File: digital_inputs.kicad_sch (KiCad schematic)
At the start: 4 parts, among them J3 Samtec Isorate, U7 SN74LV8T9541-EP

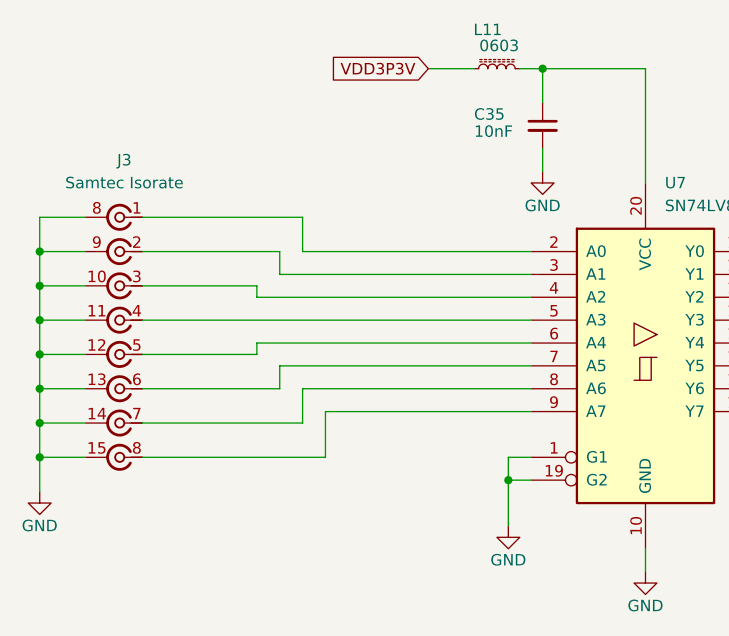
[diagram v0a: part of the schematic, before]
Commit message: Draft Schematic Complete
-See design.md for remaining design work/questions
-See output folder for current schematic prints
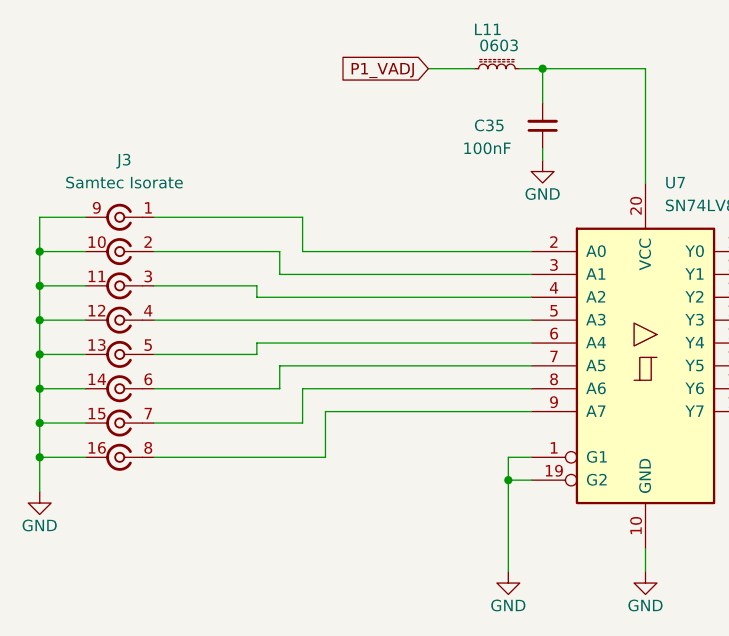
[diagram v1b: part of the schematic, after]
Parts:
- C35: value 10nF -> 100nF; footprint Capacitor_SMD:C_0603_1608Metric -> Capacitor_SMD:C_0402_1005Metric; MPN C1608C0G1E103J080AA -> GRM155R61A104KA01D; Manufacturer Samsung -> Murata
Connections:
- net GND: now also C35.1, J3.16 (gnd); no longer C35.2, J3.8 (gnd)
- net at L11.2, U7.20 (VCC): now also C35.2; no longer C35.1
- net VDD3P3V renamed P1_VADJ
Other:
- company: (none) -> Osprey DCS
- title: (none) -> RF Input FMC Board
- moved on the sheet: J3
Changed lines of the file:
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@@
 	(generator_version "9.0")
 	(paper "A5")
+	(title_block
+		(title "RF Input FMC Board")
+		(date "2025-10-01")
+		(rev "0.1")
+		(company "Osprey DCS")
+		(comment 1 "Pedro Rodriguez")
+	)
 	(junction
 		(at 96.52 81.28)
@@
 	(wire
 		(pts
+			(xy 57.15 63.5) (xy 99.06 63.5)
+		)
+		(stroke
+			(width 0)
+			(type default)
+		)
+	)
+	(wire
+		(pts
 			(xy 44.45 55.88) (xy 44.45 59.69)
 		)
@@
 		)
 	)
-	(wire
-		(pts
-			(xy 55.88 59.69) (xy 68.58 59.69)
-		)
-		(stroke
-			(width 0)
-			(type default)
-		)
-	)
 	(bus
 		(pts
@@
 	(wire
 		(pts
-			(xy 55.88 52.07) (xy 73.66 52.07)
-		)
-		(stroke
-			(width 0)
-			(type default)
-		)
-	)
-	(wire
-		(pts
-			(xy 55.88 71.12) (xy 71.12 71.12)
+			(xy 57.15 74.93) (xy 73.66 74.93)
 		)
 		(stroke
@@
 	(wire
 		(pts
+			(xy 57.15 67.31) (xy 68.58 67.31)
+		)
+		(stroke
+			(width 0)
+			(type default)
+		)
+	)
+	(wire
+		(pts
 			(xy 124.46 58.42) (xy 138.43 58.42)
 		)
@@
 	(wire
 		(pts
+			(xy 57.15 59.69) (xy 68.58 59.69)
+		)
+		(stroke
+			(width 0)
+			(type default)
+		)
+	)
+	(wire
+		(pts
 			(xy 97.79 35.56) (xy 100.33 35.56)
 		)
@@
 	(wire
 		(pts
-			(xy 96.52 81.28) (xy 96.52 86.36)
+			(xy 96.52 81.28) (xy 96.52 91.44)
 		)
 		(stroke
@@
 	(wire
 		(pts
-			(xy 55.88 67.31) (xy 68.58 67.31)
-		)
-		(stroke
-			(width 0)
-			(type default)
-		)
-	)
-	(wire
-		(pts
 			(xy 124.46 66.04) (xy 138.43 66.04)
 		)
@@
 	(wire
 		(pts
-			(xy 100.33 44.45) (xy 100.33 46.99)
-		)
-		(stroke
-			(width 0)
-			(type default)
-		)
-	)
-	(wire
-		(pts
 			(xy 99.06 73.66) (xy 76.2 73.66)
 		)
@@
 	(wire
 		(pts
-			(xy 55.88 74.93) (xy 73.66 74.93)
-		)
-		(stroke
-			(width 0)
-			(type default)
-		)
-	)
-	(wire
-		(pts
 			(xy 44.45 74.93) (xy 49.53 74.93)
 		)
@@
 	(wire
 		(pts
-			(xy 55.88 55.88) (xy 71.12 55.88)
+			(xy 100.33 44.45) (xy 100.33 45.72)
 		)
 		(stroke
@@
 	(wire
 		(pts
+			(xy 57.15 71.12) (xy 71.12 71.12)
+		)
+		(stroke
+			(width 0)
+			(type default)
+		)
+	)
+	(wire
+		(pts
+			(xy 57.15 52.07) (xy 73.66 52.07)
+		)
+		(stroke
+			(width 0)
+			(type default)
+		)
+	)
+	(wire
+		(pts
 			(xy 111.76 48.26) (xy 111.76 35.56)
 		)
@@
 	(wire
 		(pts
+			(xy 57.15 55.88) (xy 71.12 55.88)
+		)
+		(stroke
+			(width 0)
+			(type default)
+		)
+	)
+	(wire
+		(pts
 			(xy 44.45 63.5) (xy 49.53 63.5)
 		)
@@
 	(wire
 		(pts
-			(xy 55.88 78.74) (xy 76.2 78.74)
-		)
-		(stroke
-			(width 0)
-			(type default)
-		)
-	)
-	(wire
-		(pts
 			(xy 71.12 68.58) (xy 71.12 71.12)
 		)
@@
 	(wire
 		(pts
-			(xy 55.88 63.5) (xy 99.06 63.5)
+			(xy 57.15 78.74) (xy 76.2 78.74)
 		)
 		(stroke
@@
 		)
 	)
-	(global_label "VDD3P3V"
+	(global_label "P1_VADJ"
 		(shape input)
 		(at 87.63 35.56 180)
@@
 		)
 		(property "Intersheetrefs" "${INTERSHEET_REFS}"
-			(at 76.2386 35.56 0)
+			(at 76.7829 35.56 0)
 			(effects
 				(font
@@
 		(pin "15"
 		)
-		(pin "8"
+		(pin "16"
 		)
 		(pin "14"
@@
 		(lib_id "Device:C_Small")
 		(at 100.33 41.91 0)
+		(mirror x)
 		(unit 1)
 		(exclude_from_sim no)
@@
 		(dnp no)
 		(property "Reference" "C35"
-			(at 92.71 40.64 0)
+			(at 92.71 41.91 0)
 			(effects
 				(font
@@
 			)
 		)
-		(property "Value" "10nF"
-			(at 92.71 42.545 0)
+		(property "Value" "100nF"
+			(at 91.44 44.45 0)
 			(effects
 				(font
@@
 			)
 		)
-		(property "Footprint" "Capacitor_SMD:C_0603_1608Metric"
+		(property "Footprint" "Capacitor_SMD:C_0402_1005Metric"
 			(at 100.33 41.91 0)
 			(effects
@@
 			)
 		)
-		(property "MPN" "C1608C0G1E103J080AA "
+		(property "MPN" "GRM155R61A104KA01D "
 			(at 100.33 41.91 0)
 			(effects
@@
 			)
 		)
-		(property "Manufacturer" "Samsung"
+		(property "Manufacturer" "Murata"
 			(at 100.33 41.91 0)
 			(effects
@@
 	(symbol
 		(lib_id "power:GND")
-		(at 96.52 86.36 0)
+		(at 100.33 45.72 0)
+		(mirror y)
+		(unit 1)
+		(exclude_from_sim no)
+		(in_bom yes)
+		(on_board yes)
+		(dnp no)
+		(property "Reference" "#PWR023"
+			(at 100.33 52.07 0)
+			(effects
+				(font
+					(size 1.27 1.27)
+				)
+				(hide yes)
+			)
+		)
+		(property "Value" "GND"
+			(at 100.33 49.53 0)
+			(effects
+				(font
+					(size 1.27 1.27)
+				)
+			)
+		)
+		(property "Footprint" ""
+			(at 100.33 45.72 0)
+			(effects
+				(font
+					(size 1.27 1.27)
+				)
+				(hide yes)
+			)
+		)
+		(property "Datasheet" ""
+			(at 100.33 45.72 0)
+			(effects
+				(font
+					(size 1.27 1.27)
+				)
+				(hide yes)
+			)
+		)
+		(property "Description" "Power symbol creates a global label with name \"GND\" , ground"
+			(at 100.33 45.72 0)
+			(effects
+				(font
+					(size 1.27 1.27)
+				)
+				(hide yes)
+			)
+		)
+		(pin "1"
+		)
+		(instances
+			(project "rf-input-fmc"
+				(path "/1719e569-47c8-4fa0-8523-9c9686ef0dba/4cafb3fc-40db-4b97-9099-60c0c4fd2349"
+					(reference "#PWR023")
+					(unit 1)
+				)
+			)
+		)
+	)
+	(symbol
+		(lib_id "power:GND")
+		(at 96.52 91.44 0)
 		(unit 1)
 		(exclude_from_sim no)
@@
 		(dnp no)
 		(property "Reference" "#PWR022"
-			(at 96.52 92.71 0)
+			(at 96.52 97.79 0)
 			(effects
 				(font
@@
 		)
 		(property "Value" "GND"
-			(at 96.52 90.17 0)
+			(at 96.52 95.25 0)
 			(effects
 				(font
@@
 		)
 		(property "Footprint" ""
-			(at 96.52 86.36 0)
+			(at 96.52 91.44 0)
 			(effects
 				(font
@@
 		)
 		(property "Datasheet" ""
-			(at 96.52 86.36 0)
+			(at 96.52 91.44 0)
 			(effects
 				(font
@@
 		)
 		(property "Description" "Power symbol creates a global label with name \"GND\" , ground"
-			(at 96.52 86.36 0)
+			(at 96.52 91.44 0)
 			(effects
 				(font
@@
 					(unit 1)
 				)
-			)
-		)
-	)
-	(symbol
-		(lib_id "power:GND")
-		(at 100.33 46.99 0)
-		(unit 1)
-		(exclude_from_sim no)
-		(in_bom yes)
-		(on_board yes)
-		(dnp no)
-		(property "Reference" "#PWR023"
-			(at 100.33 53.34 0)
-			(effects
-				(font
-					(size 1.27 1.27)
-				)
-				(hide yes)
-			)
-		)
-		(property "Value" "GND"
-			(at 100.33 50.8 0)
-			(effects
-				(font
-					(size 1.27 1.27)
-				)
-			)
-		)
-		(property "Footprint" ""
-			(at 100.33 46.99 0)
-			(effects
-				(font
-					(size 1.27 1.27)
-				)
-				(hide yes)
-			)
-		)
-		(property "Datasheet" ""
-			(at 100.33 46.99 0)
-			(effects
-				(font
-					(size 1.27 1.27)
-				)
-				(hide yes)
-			)
-		)
-		(property "Description" "Power symbol creates a global label with name \"GND\" , ground"
-			(at 100.33 46.99 0)
-			(effects
-				(font
-					(size 1.27 1.27)
-				)
-				(hide yes)
-			)
-		)
-		(pin "1"
-		)
-		(instances
-			(project "rf-input-fmc"
-				(path "/1719e569-47c8-4fa0-8523-9c9686ef0dba/4cafb3fc-40db-4b97-9099-60c0c4fd2349"
-					(reference "#PWR023")
-					(unit 1)
-				)

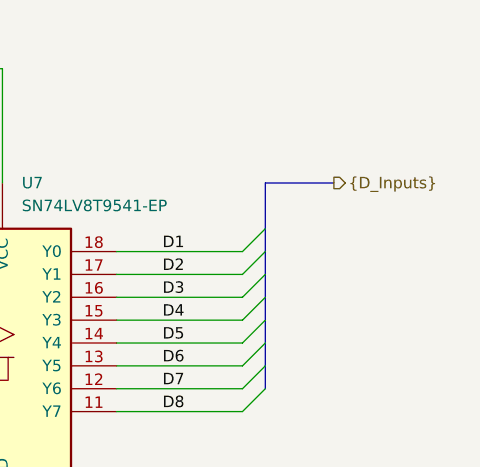
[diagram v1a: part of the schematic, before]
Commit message: fixup some hierarchical buses
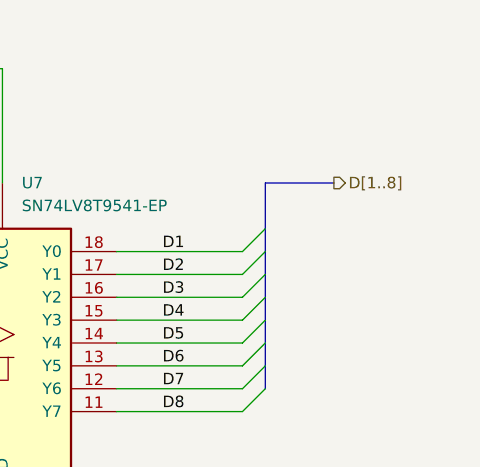
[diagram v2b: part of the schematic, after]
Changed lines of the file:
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@@
 		)
 	)
-	(hierarchical_label "{D_Inputs}"
+	(hierarchical_label "D[1..8]"
 		(shape output)
 		(at 148.59 48.26 0)

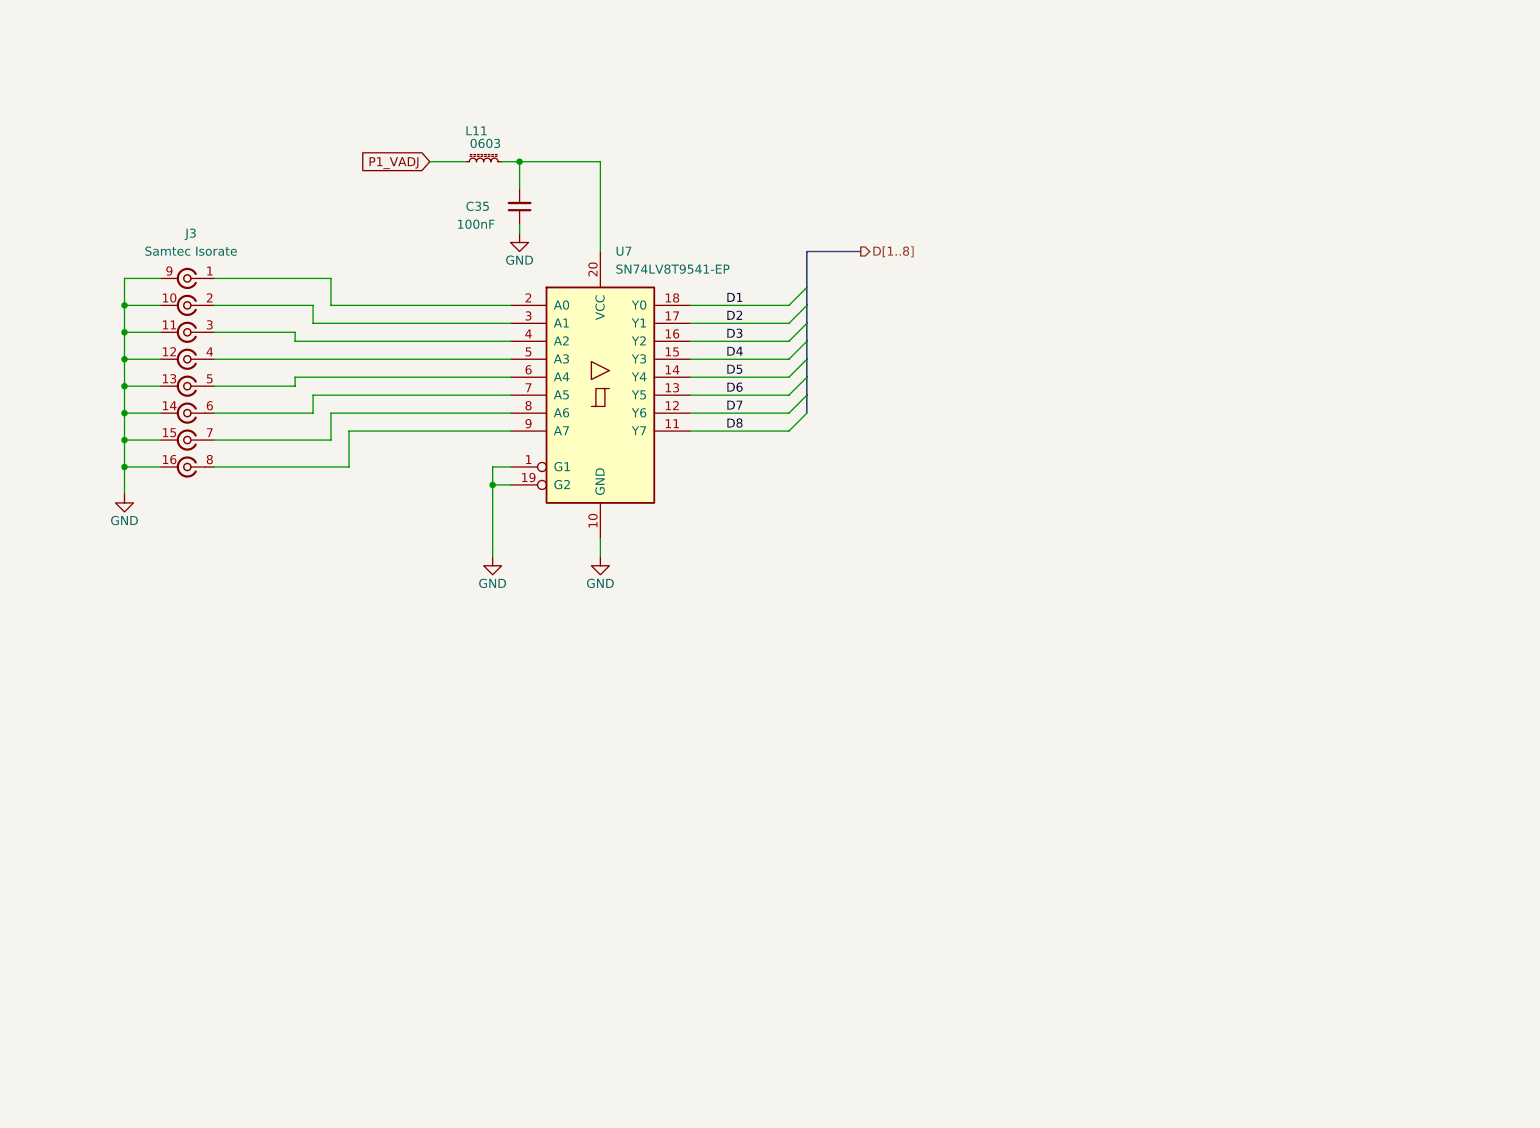
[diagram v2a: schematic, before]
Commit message: Schamtic Revision
- Added 8 more D inputs
- Removed 1 LMK01801 IC
- Cleaned up some buses
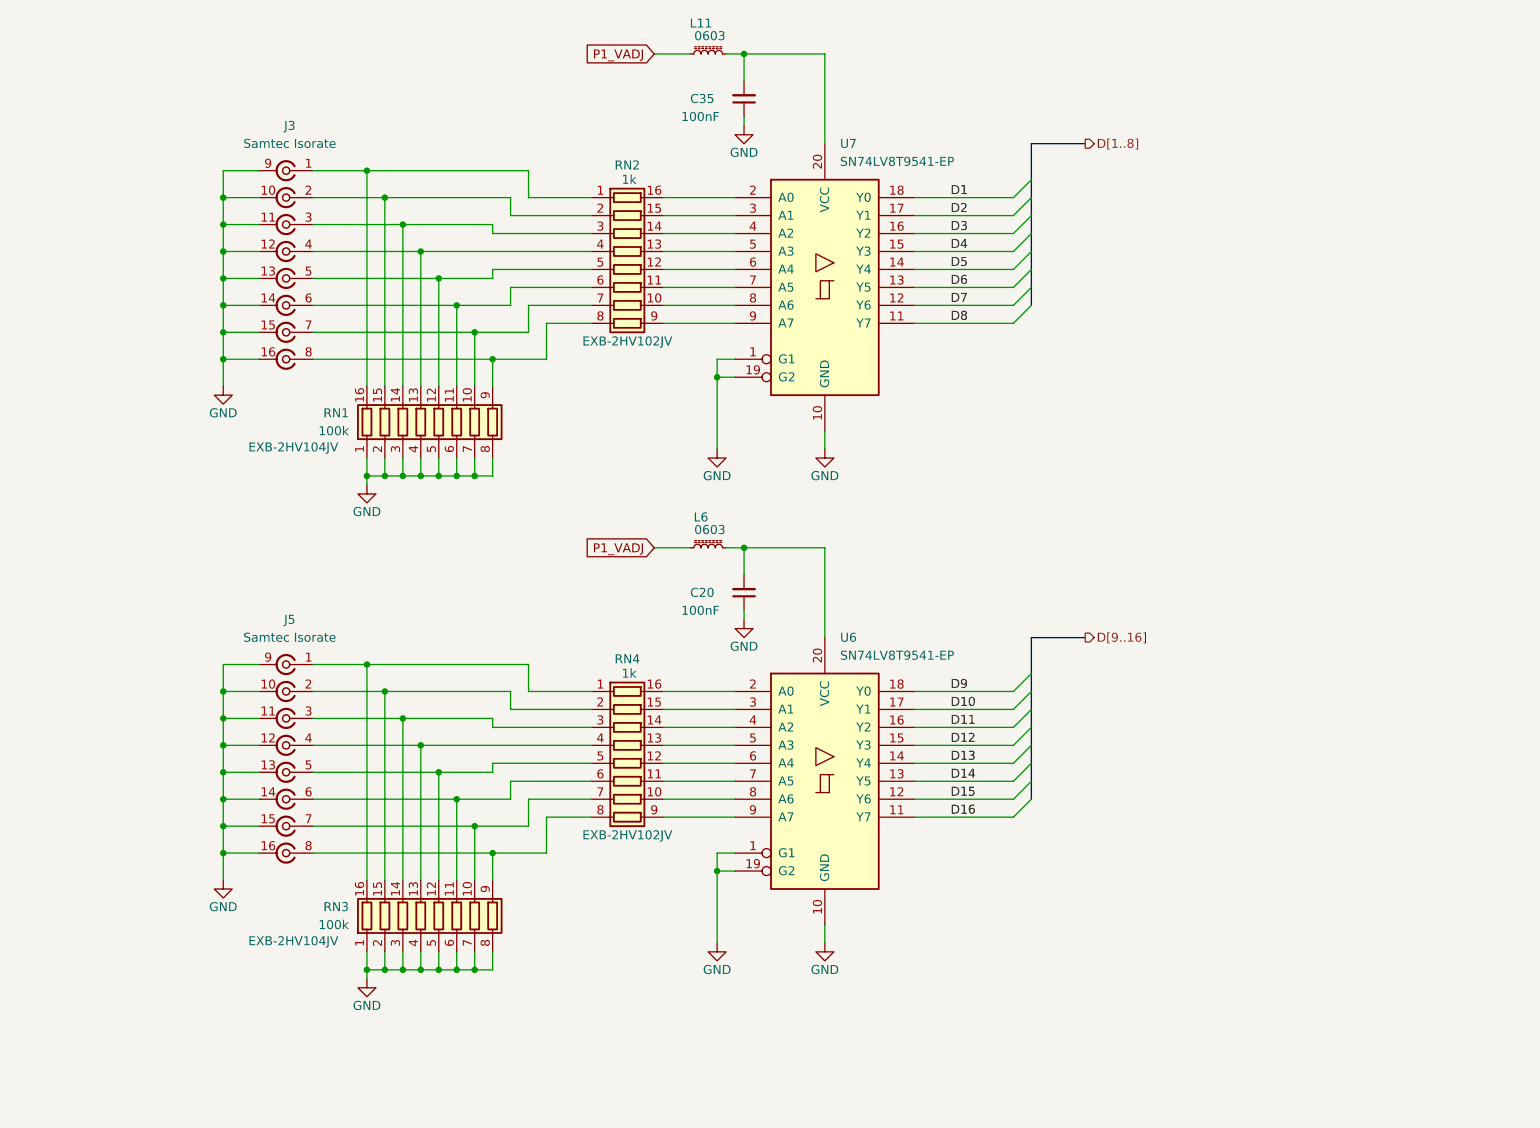
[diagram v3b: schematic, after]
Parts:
- added C20: 100nF, Capacitor_SMD:C_0402_1005Metric, symbol Device:C_Small
- added J5: Samtec Isorate, symbol rf-input-fmc:Isorate_8pin
- added L6: 0603, Inductor_SMD:L_0603_1608Metric, symbol Device:L_Ferrite_Small
- added RN1, RN3: 100k, Resistor_SMD:R_Array_Convex_8x0602, symbol Device:R_Pack08
- added RN2, RN4: 1k, Resistor_SMD:R_Array_Convex_8x0602, symbol Device:R_Pack08
- added U6: SN74LV8T9541-EP, Package_SO:TSSOP-20_4.4x6.5mm_P0.65mm, symbol 74xx:74AHC541
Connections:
- net GND: now also C20.1, J5.10 (gnd), J5.11, J5.12 (gnd), J5.13 (gnd), J5.14 (gnd), J5.15 (gnd), J5.16 (gnd), J5.9 (gnd), RN1.1 (R1.1), RN1.2 (R2.1), RN1.3 (R3.1), RN1.4 (R4.1), RN1.5 (R5.1), RN1.6 (R6.1), RN1.7 (R7.1), RN1.8 (R8.1), RN3.1 (R1.1), RN3.2 (R2.1), RN3.3 (R3.1), RN3.4 (R4.1), RN3.5 (R5.1), RN3.6 (R6.1), RN3.7 (R7.1), RN3.8 (R8.1), U6.1 (G1), U6.10 (GND), U6.19 (G2)
- net P1_VADJ: now also L6.1
- net at J3.1 (In): now also RN1.16 (R1.2), RN2.1 (R1.1); no longer U7.2 (A0)
- net at J3.2 (In): now also RN1.15 (R2.2), RN2.2 (R2.1); no longer U7.3 (A1)
- net at J3.3 (In): now also RN1.14 (R3.2), RN2.3 (R3.1); no longer U7.4 (A2)
- net at J3.4 (In): now also RN1.13 (R4.2), RN2.4 (R4.1); no longer U7.5 (A3)
- net at J3.5 (In): now also RN1.12 (R5.2), RN2.5 (R5.1); no longer U7.6 (A4)
- net at J3.6 (In): now also RN1.11 (R6.2), RN2.6 (R6.1); no longer U7.7 (A5)
- net at J3.7 (In): now also RN1.10 (R7.2), RN2.7 (R7.1); no longer U7.8 (A6)
- net at J3.8 (In): now also RN1.9 (R8.2), RN2.8 (R8.1); no longer U7.9 (A7)
- new net: J5.7 (In), RN3.10 (R7.2), RN4.7 (R7.1)
- new net: J5.6 (In), RN3.11 (R6.2), RN4.6 (R6.1)
- new net: J5.5 (In), RN3.12 (R5.2), RN4.5 (R5.1)
- new net: J5.4 (In), RN3.13 (R4.2), RN4.4 (R4.1)
- new net: J5.3 (In), RN3.14 (R3.2), RN4.3 (R3.1)
- new net: J5.2 (In), RN3.15 (R2.2), RN4.2 (R2.1)
- new net: J5.1 (In), RN3.16 (R1.2), RN4.1 (R1.1)
- new net: J5.8 (In), RN3.9 (R8.2), RN4.8 (R8.1)
- new net: RN2.16 (R1.2), U7.2 (A0)
- new net: RN2.15 (R2.2), U7.3 (A1)
- new net: RN2.14 (R3.2), U7.4 (A2)
- new net: RN2.13 (R4.2), U7.5 (A3)
- new net: RN2.12 (R5.2), U7.6 (A4)
- new net: RN2.11 (R6.2), U7.7 (A5)
- new net: RN2.10 (R7.2), U7.8 (A6)
- new net: RN2.9 (R8.2), U7.9 (A7)
- new net: RN4.10 (R7.2), U6.8 (A6)
- new net: RN4.11 (R6.2), U6.7 (A5)
- new net: RN4.12 (R5.2), U6.6 (A4)
- new net: RN4.13 (R4.2), U6.5 (A3)
- new net: RN4.14 (R3.2), U6.4 (A2)
- new net: RN4.15 (R2.2), U6.3 (A1)
- new net: RN4.16 (R1.2), U6.2 (A0)
- new net: RN4.9 (R8.2), U6.9 (A7)
- new net: C20.2, L6.2, U6.20 (VCC)
- new net D10: U6.17 (Y1)
- new net D11: U6.16 (Y2)
- new net D12: U6.15 (Y3)
- new net D13: U6.14 (Y4)
- new net D14: U6.13 (Y5)
- new net D15: U6.12 (Y6)
- new net D16: U6.11 (Y7)
- new net D9: U6.18 (Y0)
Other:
- moved on the sheet: C35, J3, L11, U7
